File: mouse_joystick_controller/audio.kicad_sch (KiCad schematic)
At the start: 0 parts

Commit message: Add DDS chip in audio sheet
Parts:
- added U7: AD9837ACPZ-RL, Janelia:DFN-10_DD_LIT-L, symbol Janelia:AD9837ACPZ-RL
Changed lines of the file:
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@@
   (title_block
     (title "mouse_joystick_controller")
-    (date "2023-06-02")
+    (date "2023-06-06")
     (rev "2.0")
     (company "Howard Hughes Medical Institute")
   )
+  (symbol (lib_id "Janelia:AD9837ACPZ-RL") (at 143.51 92.71 0) (unit 1)
+    (in_bom yes) (on_board yes) (dnp no) (fields_autoplaced)
+    (property "Reference" "U7" (at 156.21 80.01 0) (do_not_autoplace)
+      (effects (font (size 1.524 1.524)))
+    )
+    (property "Value" "AD9837ACPZ-RL" (at 143.51 92.71 0) (do_not_autoplace)
+      (effects (font (size 1.524 1.524)))
+    )
+    (property "Footprint" "Janelia:DFN-10_DD_LIT-L" (at 143.51 52.07 0)
+      (effects (font (size 1.27 1.27) italic) hide)
+    )
+    (property "Datasheet" "" (at 107.95 58.42 0)
+      (effects (font (size 1.27 1.27) italic) hide)
+    )
+    (property "Description" "IC DDS 5MHZ 10BIT" (at 143.51 59.69 0)
+      (effects (font (size 1.27 1.27)) hide)
+    )
+    (property "Package" " 10LFCSP" (at 143.51 46.99 0)
+      (effects (font (size 1.27 1.27)) hide)
+    )
+    (property "Manufacturer" "Analog Devices Inc." (at 143.51 44.45 0)
+      (effects (font (size 1.27 1.27)) hide)
+    )
+    (property "Manufacturer Part Number" "AD9837ACPZ-RL" (at 143.51 49.53 0)
+      (effects (font (size 1.27 1.27)) hide)
+    )
+    (property "Vendor" "Digi-Key" (at 143.51 54.61 0)
+      (effects (font (size 1.27 1.27)) hide)
+    )
+    (property "Vendor Part Number" "AD9837ACPZ-RLCT-ND" (at 143.51 57.15 0)
+      (effects (font (size 1.27 1.27)) hide)
+    )
+    (pin "1")
+    (pin "10")
+    (pin "11")
+    (pin "2")
+    (pin "3")
+    (pin "4")
+    (pin "5")
+    (pin "6")
+    (pin "7")
+    (pin "8")
+    (pin "9")
+    (instances
+      (project "mouse_joystick_controller"
+        (path "/cc457ebc-4af6-4663-b19f-8cb38f061cb4/0ca0d34b-2b7f-42eb-8f7f-77dbfc402b19"
+          (reference "U7") (unit 1)
+        )
+      )
+    )
+  )
 )

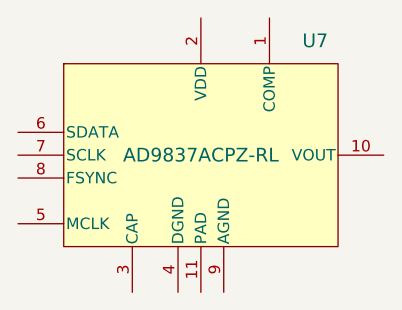
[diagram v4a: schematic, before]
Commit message: Test pin rcpt
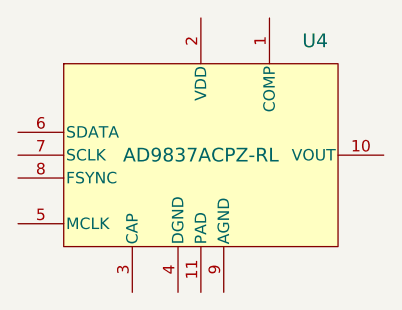
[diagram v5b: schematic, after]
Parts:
- renumbered U7 to U4
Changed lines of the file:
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@@
   (title_block
     (title "mouse_joystick_controller")
-    (date "2023-06-07")
+    (date "2023-06-09")
     (rev "2.0")
     (company "Howard Hughes Medical Institute")
@@
   (symbol (lib_id "Janelia:AD9837ACPZ-RL") (at 143.51 92.71 0) (unit 1)
     (in_bom yes) (on_board yes) (dnp no) (fields_autoplaced)
-    (property "Reference" "U7" (at 156.21 80.01 0) (do_not_autoplace)
+    (property "Reference" "U4" (at 156.21 80.01 0) (do_not_autoplace)
       (effects (font (size 1.524 1.524)))
     )
@@
       (effects (font (size 1.27 1.27)) hide)
     )
+    (property "Sim.Enable" "0" (at 143.51 92.71 0)
+      (effects (font (size 1.27 1.27)) hide)
+    )
     (pin "1")
     (pin "10")
@@
       (project "mouse_joystick_controller"
         (path "/cc457ebc-4af6-4663-b19f-8cb38f061cb4/0ca0d34b-2b7f-42eb-8f7f-77dbfc402b19"
-          (reference "U7") (unit 1)
+          (reference "U4") (unit 1)
         )
       )
